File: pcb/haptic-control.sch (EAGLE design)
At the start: 145 parts, among them M1 SPH0641LM4H-1, P1 2P-PAD_1X3.5, P2 2P-PAD_1X3.5, P3 2P-PAD_1X3.5, P4 2P-PAD_1X3.5, U1 MIC23159, U10 DRV2605L, U11 DRV2605L, U12 MTCH6301, U2 BQ51050B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

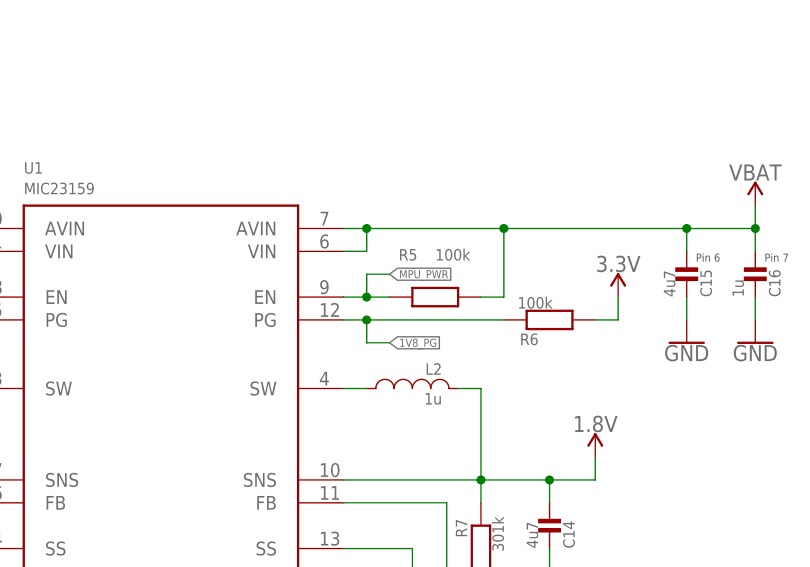
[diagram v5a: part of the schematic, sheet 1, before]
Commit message: removed hardware MPU pwr switch
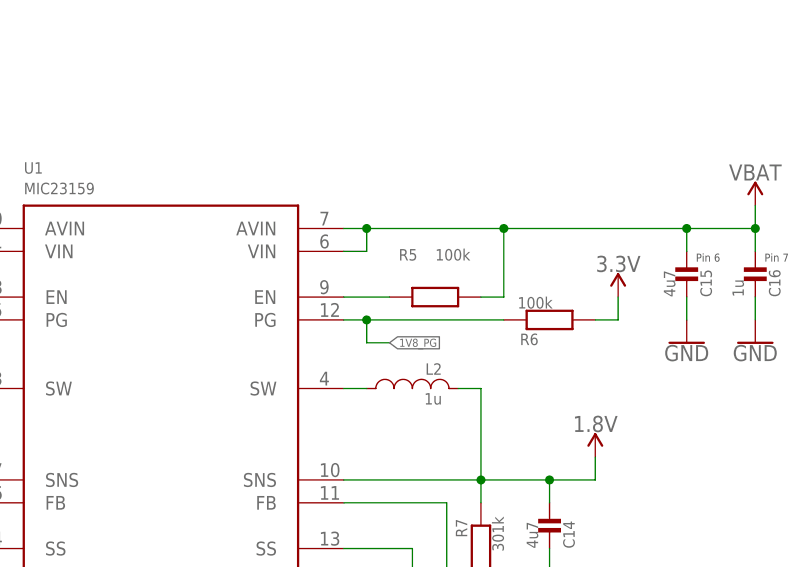
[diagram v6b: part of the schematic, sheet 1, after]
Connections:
- net MPU_PWR: no longer U5.DIO_15, U9.EN
- net N$11: now also U9.EN
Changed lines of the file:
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@@
 <pinref part="R5" gate="G$1" pin="P$1"/>
 <pinref part="U1" gate="G$1" pin="EN@1"/>
-<wire x1="119.38" y1="205.74" x2="116.84" y2="205.74" width="0.1524" layer="91"/>
-<wire x1="116.84" y1="205.74" x2="114.3" y2="205.74" width="0.1524" layer="91"/>
-<wire x1="116.84" y1="205.74" x2="116.84" y2="208.28" width="0.1524" layer="91"/>
-<junction x="116.84" y="205.74"/>
-<wire x1="116.84" y1="208.28" x2="119.38" y2="208.28" width="0.1524" layer="91"/>
-<label x="119.38" y="208.28" size="0.889" layer="95" xref="yes"/>
+<wire x1="119.38" y1="205.74" x2="114.3" y2="205.74" width="0.1524" layer="91"/>
 </segment>
 </net>
@@
 </segment>
 </net>
-<net name="MPU_PWR" class="0">
-<segment>
-<wire x1="251.46" y1="111.76" x2="254" y2="111.76" width="0.1524" layer="91"/>
-<label x="254" y="111.76" size="0.889" layer="95" xref="yes"/>
-<pinref part="U5" gate="G$1" pin="DIO_15"/>
-</segment>
-</net>
 <net name="FSR_CH_P" class="0">
 <segment>
@@
 <wire x1="279.4" y1="124.46" x2="279.4" y2="149.86" width="0.1524" layer="91"/>
 <wire x1="279.4" y1="149.86" x2="269.24" y2="149.86" width="0.1524" layer="91"/>
-</segment>
-</net>
-<net name="MPU_PWR" class="0">
-<segment>
-<wire x1="264.16" y1="147.32" x2="266.7" y2="147.32" width="0.1524" layer="91"/>
-<label x="266.7" y="147.32" size="0.889" layer="95" xref="yes"/>
 <pinref part="U9" gate="G$1" pin="EN"/>
-</segment>
-</net>
+<wire x1="264.16" y1="147.32" x2="269.24" y2="147.32" width="0.1524" layer="91"/>
+<wire x1="269.24" y1="147.32" x2="269.24" y2="149.86" width="0.1524" layer="91"/>
+</segment>
+</net>

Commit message: Nothing to do Needs revision
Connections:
- net FSR_CH_N renamed FSR_2
- removed net FSR_CH_P: C51.P$1, R29.1, R30.P$2, U5.DIO_26
- removed net FSR_VOL_N: C56.P$1, R35.2, R36.P$2, U5.DIO_24
- removed net FSR_VOL_P: C55.P$1, R33.2, R34.P$2, U5.DIO_27
- new net FSR_1: C51.P$1, R29.1, R30.P$2, U5.DIO_24
- new net FSR_3: C55.P$1, R33.2, R34.P$2, U5.DIO_26
- new net FSR_4: C56.P$1, R35.2, R36.P$2, U5.DIO_27
- net !QI_CHG: now also U5.DIO_13; no longer U5.DIO_12
- net 1V8_PG: now also U5.DIO_28; no longer U5.DIO_14
- net I2S_CLK: now also U5.DIO_21; no longer U5.DIO_20
- net I2S_DATIN: now also U5.DIO_20; no longer U5.DIO_19
- net LRA_EN: now also U5.DIO_8; no longer U5.DIO_1
- net MPU_INT: now also U5.DIO_22; no longer U5.DIO_18
- net QI_CTRL: now also U5.DIO_12; no longer U5.DIO_13
- net SCL: no longer R23.P$1
- net SDA: now also R23.P$1
- net TC_!RESET: now also U5.DIO_18; no longer U5.DIO_21
- net TC_INT: now also U5.DIO_19; no longer U5.DIO_22
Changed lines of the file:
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@@
 <?xml version="1.0" encoding="utf-8"?>
 <!DOCTYPE eagle SYSTEM "eagle.dtd">
-<eagle version="9.3.2">
+<eagle version="9.3.0">
 <drawing>
 <settings>
@@
 </segment>
 <segment>
-<label x="284.48" y="154.94" size="0.889" layer="95" rot="R270" xref="yes"/>
-<wire x1="284.48" y1="157.48" x2="284.48" y2="154.94" width="0.1524" layer="91"/>
-<pinref part="R23" gate="G$1" pin="P$1"/>
-</segment>
-<segment>
 <label x="254" y="127" size="0.889" layer="95" xref="yes"/>
 <wire x1="251.46" y1="127" x2="254" y2="127" width="0.1524" layer="91"/>
@@
 </segment>
 </net>
-<net name="I2S_CLK" class="0">
-<segment>
-<wire x1="251.46" y1="99.06" x2="254" y2="99.06" width="0.1524" layer="91"/>
-<label x="254" y="99.06" size="0.889" layer="95" xref="yes"/>
-<pinref part="U5" gate="G$1" pin="DIO_20"/>
-</segment>
-</net>
-<net name="I2S_DATIN" class="0">
-<segment>
-<wire x1="251.46" y1="101.6" x2="254" y2="101.6" width="0.1524" layer="91"/>
-<label x="254" y="101.6" size="0.889" layer="95" xref="yes"/>
-<pinref part="U5" gate="G$1" pin="DIO_19"/>
-</segment>
-</net>
 <net name="N$12" class="0">
 <segment>
@@
 </segment>
 </net>
-<net name="1V8_PG" class="0">
-<segment>
-<wire x1="251.46" y1="114.3" x2="254" y2="114.3" width="0.1524" layer="91"/>
-<label x="254" y="114.3" size="0.889" layer="95" rot="MR180" xref="yes"/>
-<pinref part="U5" gate="G$1" pin="DIO_14"/>
-</segment>
-</net>
-<net name="FSR_CH_P" class="0">
+<net name="FSR_1" class="0">
 <segment>
-<wire x1="208.28" y1="142.24" x2="205.74" y2="142.24" width="0.1524" layer="91"/>
-<label x="205.74" y="142.24" size="0.889" layer="95" rot="R180" xref="yes"/>
-<pinref part="U5" gate="G$1" pin="DIO_26"/>
+<wire x1="208.28" y1="147.32" x2="205.74" y2="147.32" width="0.1524" layer="91"/>
+<label x="205.74" y="147.32" size="0.889" layer="95" rot="R180" xref="yes"/>
+<pinref part="U5" gate="G$1" pin="DIO_24"/>
 </segment>
 </net>
-<net name="FSR_CH_N" class="0">
+<net name="FSR_2" class="0">
 <segment>
 <wire x1="208.28" y1="144.78" x2="205.74" y2="144.78" width="0.1524" layer="91"/>
@@
 </segment>
 </net>
-<net name="FSR_VOL_P" class="0">
+<net name="FSR_3" class="0">
 <segment>
-<wire x1="208.28" y1="139.7" x2="205.74" y2="139.7" width="0.1524" layer="91"/>
-<label x="205.74" y="139.7" size="0.889" layer="95" rot="R180" xref="yes"/>
-<pinref part="U5" gate="G$1" pin="DIO_27"/>
-</segment>
-</net>
-<net name="FSR_VOL_N" class="0">
-<segment>
-<wire x1="208.28" y1="147.32" x2="205.74" y2="147.32" width="0.1524" layer="91"/>
-<label x="205.74" y="147.32" size="0.889" layer="95" rot="R180" xref="yes"/>
-<pinref part="U5" gate="G$1" pin="DIO_24"/>
+<wire x1="208.28" y1="142.24" x2="205.74" y2="142.24" width="0.1524" layer="91"/>
+<label x="205.74" y="142.24" size="0.889" layer="95" rot="R180" xref="yes"/>
+<pinref part="U5" gate="G$1" pin="DIO_26"/>
 </segment>
 </net>
@@
 </segment>
 </net>
-<net name="!QI_CHG" class="0">
+<net name="SDA" class="0">
 <segment>
-<wire x1="251.46" y1="119.38" x2="254" y2="119.38" width="0.1524" layer="91"/>
-<label x="254" y="119.38" size="0.889" layer="95" xref="yes"/>
-<pinref part="U5" gate="G$1" pin="DIO_12"/>
+<label x="254" y="124.46" size="0.889" layer="95" xref="yes"/>
+<wire x1="251.46" y1="124.46" x2="254" y2="124.46" width="0.1524" layer="91"/>
+<pinref part="U5" gate="G$1" pin="DIO_10"/>
+</segment>
+<segment>
+<label x="284.48" y="154.94" size="0.889" layer="95" rot="R270" xref="yes"/>
+<wire x1="284.48" y1="157.48" x2="284.48" y2="154.94" width="0.1524" layer="91"/>
+<pinref part="R23" gate="G$1" pin="P$1"/>
 </segment>
 </net>
-<net name="QI_CTRL" class="0">
+<net name="VBAT_SNS" class="0">
 <segment>
-<wire x1="251.46" y1="116.84" x2="254" y2="116.84" width="0.1524" layer="91"/>
-<label x="254" y="116.84" size="0.889" layer="95" xref="yes"/>
-<pinref part="U5" gate="G$1" pin="DIO_13"/>
+<wire x1="208.28" y1="149.86" x2="205.74" y2="149.86" width="0.1524" layer="91"/>
+<label x="205.74" y="149.86" size="0.889" layer="95" rot="R180" xref="yes"/>
+<pinref part="U5" gate="G$1" pin="DIO_23"/>
 </segment>
 </net>
-<net name="MPU_INT" class="0">
+<net name="FSR_4" class="0">
 <segment>
-<wire x1="251.46" y1="104.14" x2="254" y2="104.14" width="0.1524" layer="91"/>
-<label x="254" y="104.14" size="0.889" layer="95" xref="yes"/>
-<pinref part="U5" gate="G$1" pin="DIO_18"/>
+<wire x1="208.28" y1="139.7" x2="205.74" y2="139.7" width="0.1524" layer="91"/>
+<label x="205.74" y="139.7" size="0.889" layer="95" rot="R180" xref="yes"/>
+<pinref part="U5" gate="G$1" pin="DIO_27"/>
 </segment>
 </net>
-<net name="TC_!RESET" class="0">
+<net name="1V8_PG" class="0">
+<segment>
+<wire x1="208.28" y1="137.16" x2="205.74" y2="137.16" width="0.1524" layer="91"/>
+<label x="205.74" y="137.16" size="0.889" layer="95" rot="MR0" xref="yes"/>
+<pinref part="U5" gate="G$1" pin="DIO_28"/>
+</segment>
+</net>
+<net name="I2S_CLK" class="0">
 <segment>
 <wire x1="251.46" y1="96.52" x2="254" y2="96.52" width="0.1524" layer="91"/>
@@
 </segment>
 </net>
-<net name="TC_INT" class="0">
+<net name="I2S_DATIN" class="0">
+<segment>
+<wire x1="251.46" y1="99.06" x2="254" y2="99.06" width="0.1524" layer="91"/>
+<label x="254" y="99.06" size="0.889" layer="95" xref="yes"/>
+<pinref part="U5" gate="G$1" pin="DIO_20"/>
+</segment>
+</net>
+<net name="MPU_INT" class="0">
 <segment>
 <wire x1="251.46" y1="93.98" x2="254" y2="93.98" width="0.1524" layer="91"/>
@@
 </segment>
 </net>
-<net name="SDA" class="0">
+<net name="TC_!RESET" class="0">
 <segment>
-<label x="254" y="124.46" size="0.889" layer="95" xref="yes"/>
-<wire x1="251.46" y1="124.46" x2="254" y2="124.46" width="0.1524" layer="91"/>
-<pinref part="U5" gate="G$1" pin="DIO_10"/>
+<wire x1="251.46" y1="104.14" x2="254" y2="104.14" width="0.1524" layer="91"/>
+<label x="254" y="104.14" size="0.889" layer="95" xref="yes"/>
+<pinref part="U5" gate="G$1" pin="DIO_18"/>
 </segment>
 </net>
-<net name="VBAT_SNS" class="0">
+<net name="TC_INT" class="0">
 <segment>
-<wire x1="208.28" y1="149.86" x2="205.74" y2="149.86" width="0.1524" layer="91"/>
-<label x="205.74" y="149.86" size="0.889" layer="95" rot="R180" xref="yes"/>
-<pinref part="U5" gate="G$1" pin="DIO_23"/>
+<wire x1="251.46" y1="101.6" x2="254" y2="101.6" width="0.1524" layer="91"/>
+<label x="254" y="101.6" size="0.889" layer="95" xref="yes"/>
+<pinref part="U5" gate="G$1" pin="DIO_19"/>
+</segment>
+</net>
+<net name="!QI_CHG" class="0">
+<segment>
+<wire x1="251.46" y1="116.84" x2="254" y2="116.84" width="0.1524" layer="91"/>
+<label x="254" y="116.84" size="0.889" layer="95" xref="yes"/>
+<pinref part="U5" gate="G$1" pin="DIO_13"/>
+</segment>
+</net>
+<net name="QI_CTRL" class="0">
+<segment>
+<wire x1="251.46" y1="119.38" x2="254" y2="119.38" width="0.1524" layer="91"/>
+<label x="254" y="119.38" size="0.889" layer="95" xref="yes"/>
+<pinref part="U5" gate="G$1" pin="DIO_12"/>
 </segment>
 </net>
 <net name="LRA_EN" class="0">
 <segment>
-<wire x1="251.46" y1="147.32" x2="254" y2="147.32" width="0.1524" layer="91"/>
-<label x="254" y="147.32" size="0.889" layer="95" xref="yes"/>
-<pinref part="U5" gate="G$1" pin="DIO_1"/>
+<wire x1="251.46" y1="129.54" x2="254" y2="129.54" width="0.1524" layer="91"/>
+<label x="254" y="129.54" size="0.889" layer="95" xref="yes"/>
+<pinref part="U5" gate="G$1" pin="DIO_8"/>
 </segment>
 </net>
@@
 </segment>
 </net>
-<net name="FSR_CH_P" class="0">
+<net name="FSR_1" class="0">
 <segment>
 <wire x1="40.64" y1="144.78" x2="40.64" y2="142.24" width="0.1524" layer="91"/>
@@
 </segment>
 </net>
-<net name="FSR_CH_N" class="0">
+<net name="FSR_2" class="0">
 <segment>
 <wire x1="83.82" y1="144.78" x2="83.82" y2="142.24" width="0.1524" layer="91"/>
@@
 </segment>
 </net>
-<net name="FSR_VOL_P" class="0">
+<net name="FSR_3" class="0">
 <segment>
 <wire x1="124.46" y1="144.78" x2="127" y2="144.78" width="0.1524" layer="91"/>
@@
 </segment>
 </net>
-<net name="FSR_VOL_N" class="0">
+<net name="FSR_4" class="0">
 <segment>
 <wire x1="170.18" y1="144.78" x2="172.72" y2="144.78" width="0.1524" layer="91"/>

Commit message: finished routing
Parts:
- added C62: 10u, Passive Components > Capacitors > Multilayer Ceramic Capacitors MLCC:MLCC0603
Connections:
- net GND: now also C62.P$2
- net VBAT: now also C62.P$1
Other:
- note added: "Antena & Balun"
- note removed: "Antena & Ballun"
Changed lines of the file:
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@@
 <?xml version="1.0" encoding="utf-8"?>
 <!DOCTYPE eagle SYSTEM "eagle.dtd">
-<eagle version="9.3.0">
+<eagle version="9.3.2">
 <drawing>
 <settings>
@@
 <part name="MAT-Y9" library="Touch Panel" deviceset="Y_4P" device=""/>
 <part name="LOGO1" library="Silkscreen" deviceset="IPL" device="-10MM"/>
+<part name="GND88" library="Utility &gt; Power Symbols" deviceset="GND" device=""/>
+<part name="SUPPLY50" library="Utility &gt; Power Symbols" deviceset="VBAT" device=""/>
+<part name="C62" library="Passive Components &gt; Capacitors &gt; Multilayer Ceramic Capacitors MLCC" deviceset="MLCC" device="0603" value="10u"/>
 </parts>
 <sheets>
@@
 <text x="165.1" y="43.18" size="3.81" layer="97">MCU</text>
 <text x="307.34" y="99.06" size="3.81" layer="97">Clocks</text>
-<text x="12.7" y="76.2" size="3.81" layer="97">Antena &amp; Ballun</text>
+<text x="12.7" y="76.2" size="3.81" layer="97">Antena &amp; Balun</text>
 <text x="12.7" y="10.16" size="3.81" layer="97">Debugging</text>
 <text x="82.296" y="8.128" size="1.778" layer="97">When the Jumpers are Connected
@@
 <attribute name="NAME" x="144.78" y="85.09" size="1.778" layer="95" ratio="10" rot="SR0" align="top-left"/>
 </instance>
+<instance part="GND88" gate="1" x="93.98" y="213.36" smashed="yes">
+<attribute name="VALUE" x="93.98" y="213.106" size="1.778" layer="96" align="top-center"/>
+</instance>
+<instance part="SUPPLY50" gate="G$1" x="93.98" y="226.06" smashed="yes">
+<attribute name="VALUE" x="93.98" y="228.854" size="1.778" layer="96" align="bottom-center"/>
+</instance>
+<instance part="C62" gate="G$1" x="93.98" y="220.98" smashed="yes">
+<attribute name="NAME" x="92.456" y="218.44" size="1.27" layer="95" rot="R90"/>
+<attribute name="VALUE" x="96.52" y="218.44" size="1.27" layer="96" rot="R90"/>
+</instance>
 </instances>
 <busses>
@@
 <wire x1="180.34" y1="129.54" x2="180.34" y2="127" width="0.1524" layer="91"/>
 </segment>
+<segment>
+<pinref part="GND88" gate="1" pin="GND"/>
+<wire x1="93.98" y1="218.44" x2="93.98" y2="215.9" width="0.1524" layer="91"/>
+<pinref part="C62" gate="G$1" pin="P$2"/>
+</segment>
 </net>
 <net name="3.3V" class="0">
@@
 <pinref part="C53" gate="G$1" pin="P$1"/>
 </segment>
+<segment>
+<wire x1="93.98" y1="223.52" x2="93.98" y2="226.06" width="0.1524" layer="91"/>
+<pinref part="SUPPLY50" gate="G$1" pin="VBAT"/>
+<pinref part="C62" gate="G$1" pin="P$1"/>
+</segment>
 </net>
